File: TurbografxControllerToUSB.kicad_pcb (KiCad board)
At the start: 2 copper layers, 39.6 x 45.3 mm, 13 parts, among them CON1 AVR-ISP6, J1 USB, J2 DB9, U1 ATMEGA32U2-AU, X1 16Mhz

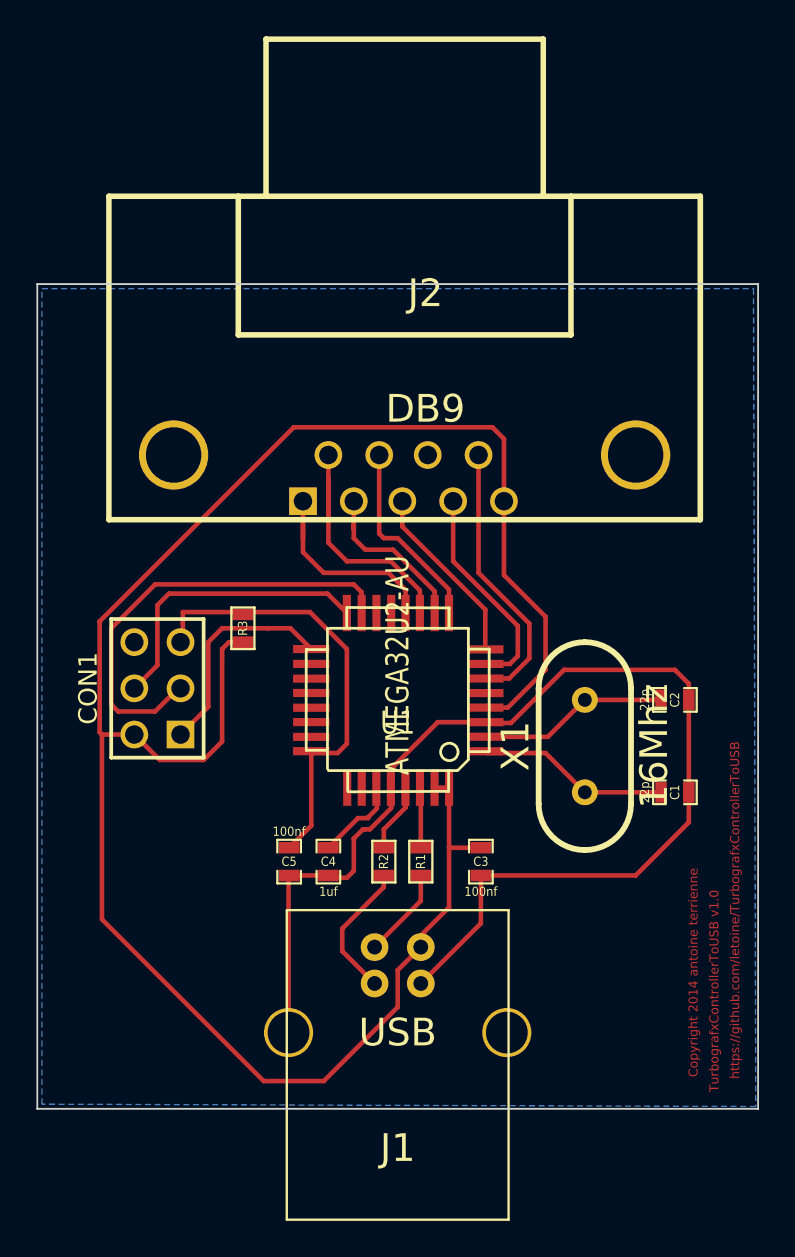
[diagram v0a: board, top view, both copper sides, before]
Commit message: Adding DIN8 component.
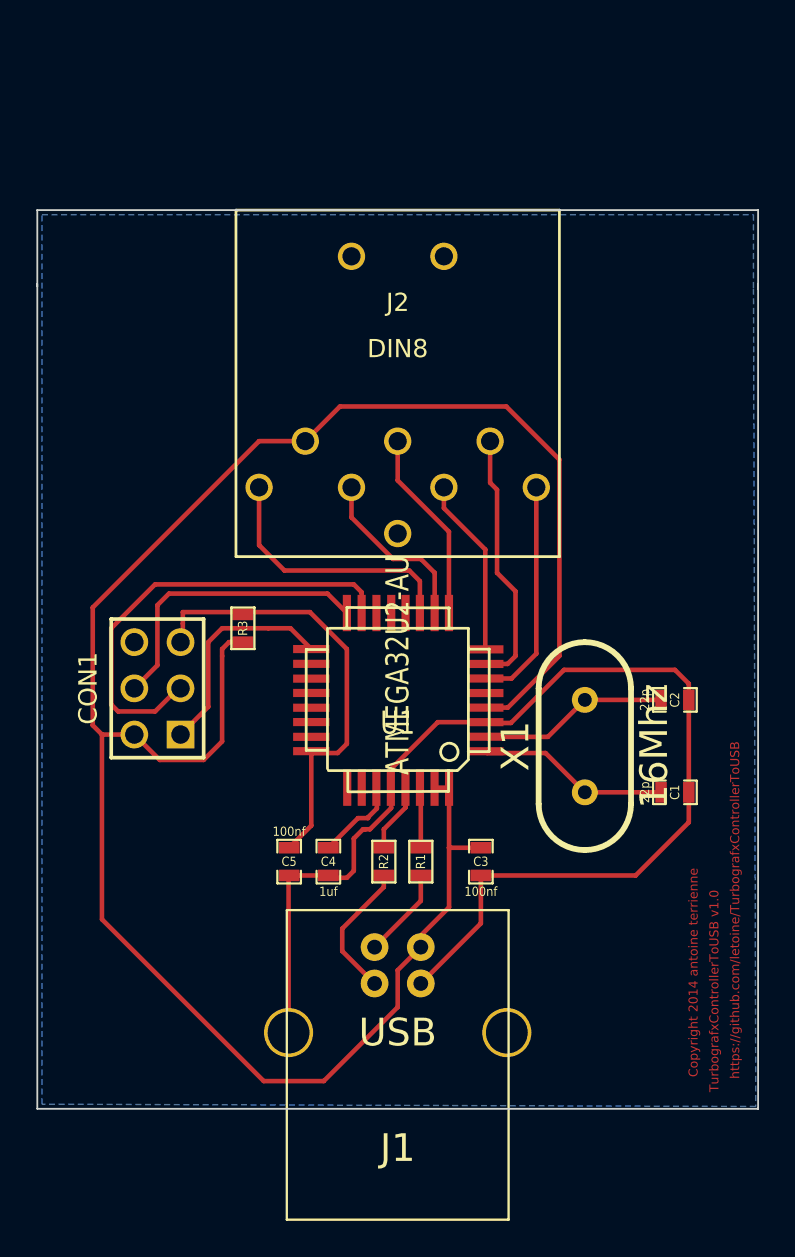
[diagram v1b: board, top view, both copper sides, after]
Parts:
- J2: value DB9 -> DIN8; footprint DB9FC -> DIN-8-FEMALE
- moved J2 4.58 mm to (210.6, 126.7), turned to 180 degrees
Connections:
- net C_START_BUTTON renamed DATA_SELECT
- J2 pad 1: UP_Z -> VCC
- J2 pad 2: DOWN_Y -> UP_I_BUTTON
- J2 pad 3: LEFT_X -> RIGHT_II_BUTTON
- J2 pad 4: RIGHT_MODE -> DOWN_SELECT_BUTTON
- J2 pad 5: VCC -> LEFT_RUN_BUTTON
- J2 pad 7: SELECT_CLK -> ~OE~
- J2 pad 9: B_A_BUTTON -> (no net)
- U1 pad 10: DOWN_Y -> DOWN_SELECT_BUTTON
- U1 pad 12: UP_Z -> (no net)
- U1 pad 6: B_A_BUTTON -> ~OE~
- U1 pad 7: RIGHT_MODE -> RIGHT_II_BUTTON
- U1 pad 8: LEFT_X -> LEFT_RUN_BUTTON
- U1 pad 9: SELECT_CLK -> UP_I_BUTTON
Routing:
- net B_A_BUTTON: track 15.2 -> 0.00 mm
- net RIGHT_II_BUTTON: track 0.00 -> 14.2 mm
- net ~OE~: track 0.00 -> 12.5 mm
- net RIGHT_MODE: track 12.0 -> 0.00 mm
- net UP_Z: track 11.3 -> 0.00 mm
- net SELECT_CLK: track 10.7 -> 0.00 mm
- net UP_I_BUTTON: track 0.00 -> 10.6 mm
- net LEFT_X: track 10.0 -> 0.00 mm
- net LEFT_RUN_BUTTON: track 0.00 -> 9.85 mm
- net DOWN_SELECT_BUTTON: track 0.00 -> 9.70 mm
- net DOWN_Y: track 9.13 -> 0.00 mm
- net VCC: track 112.7 -> 116.4 mm
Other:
- board size 39.6 x 45.3 mm -> 39.6 x 49.4 mm
